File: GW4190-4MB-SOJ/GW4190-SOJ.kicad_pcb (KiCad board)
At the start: 4 copper layers, 88.9 x 20.3 mm, 10 parts, among them J1 DRAM-SIMM-30, U1 4C4M4, U2 4C4M4

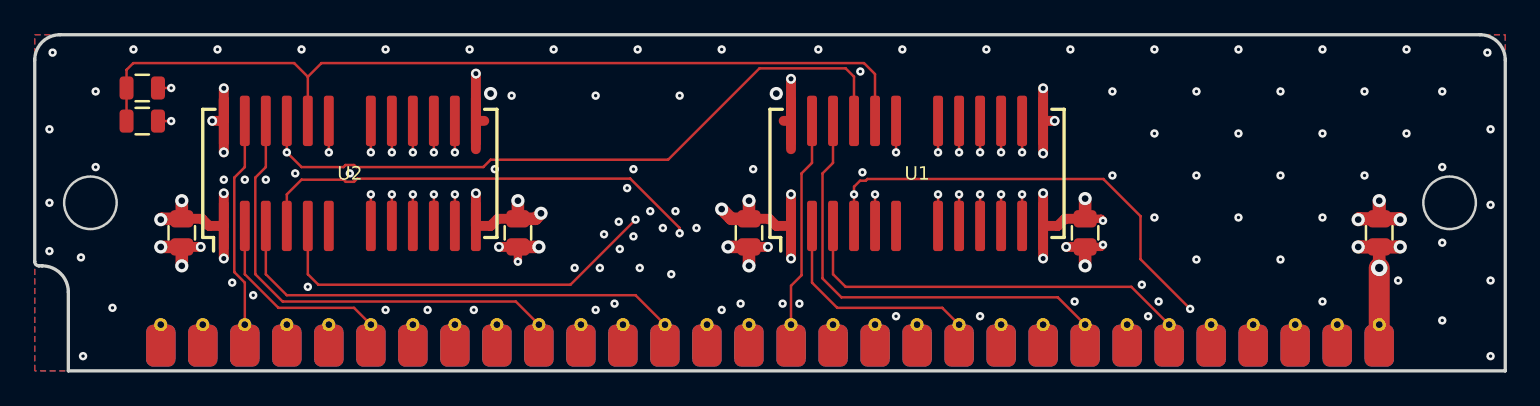
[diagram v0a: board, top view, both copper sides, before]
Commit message: Update to KiCAD 6
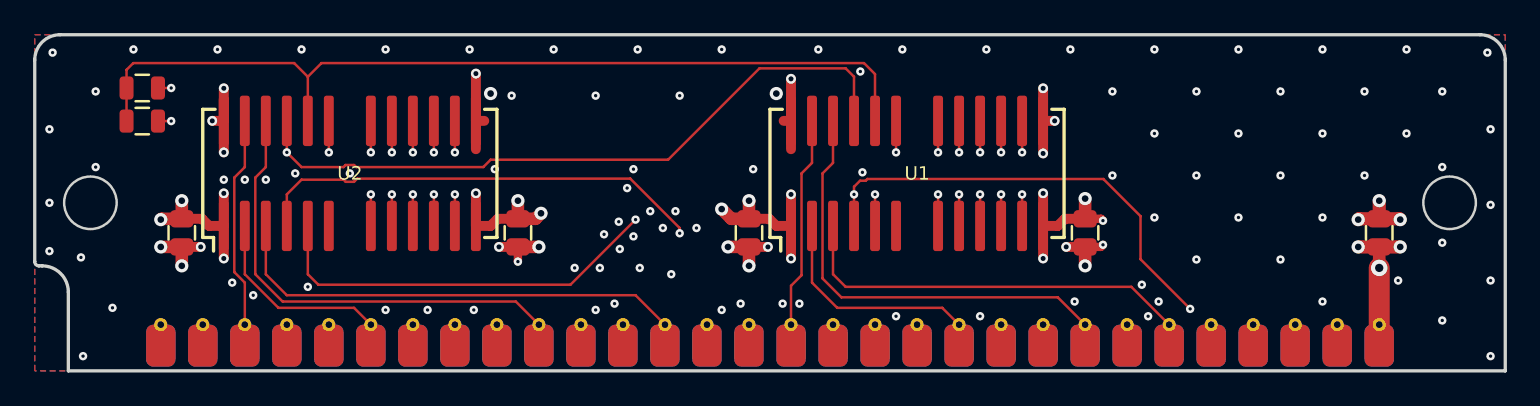
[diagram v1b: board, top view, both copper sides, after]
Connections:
- net /~CASP~ renamed /~{CASP}
- net /~CAS~ renamed /~{CAS}
- net /~OE~ renamed /~{OE}
- net /~RAS~ renamed /~{RAS}
- net /~WE~ renamed /~{WE}
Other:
- net class Default removed
